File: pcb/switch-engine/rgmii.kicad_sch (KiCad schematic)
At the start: 64 parts, among them J20 0826-1G1T-23-F, Q2 SSM6N58NU, U22 ECS-1612MV-250-CN, U23 KSZ9031RN, U24 ESD224DQAR, U26 ESD224DQAR, U8 XILINX_ULTRASCALEPLUS_B676

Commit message: First iteration of main board PCB schematic is now passing ERC
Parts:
- added C143: 0.47 uF, azonenberg_pcb:EIA_0402_CAP_NOSILK, symbol device:C
- added C144, C145: 0.1 uF, azonenberg_pcb:EIA_0402_CAP_NOSILK, symbol device:C
- added U27: SIT9121AI-2BF-XXS156.250000G, azonenberg_pcb:OSCILLATOR_LVDS_3.2x2.5, symbol osc-azonenberg:OSC_LVDS_NOPAD
- U8: value XILINX_ULTRASCALEPLUS_B676 -> XCKU5P-2FFVB676I
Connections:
- net 3V3: now also C143.1, U27.1 (EN), U27.6 (VDD)
- net GND: now also C143.2, U27.3 (GND)
- net FPGA_CLK_156M25_P: now reaches U8.D19 (IO_L12P_T1U_N10_GC_67)
- net FPGA_CLK_156M25_P: now also C144.2
- net FPGA_CLK_156M25_N: now reaches U8.D20 (IO_L12N_T1U_N11_GC_67)
- net FPGA_CLK_156M25_N: now also C145.2
- new net RC3_N: C145.1, U27.5 (OUT_N)
- new net RC3_P: C144.1, U27.4 (OUT_P)
- no-connect marks 37 -> 35
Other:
- note added: "Clocks"
- note added: "FPGA RGMII"
- note added: "PHY and straps"
- note added: "PHY decoupling"
- note added: "RJ45 and ESD protection"
- note removed: "TODO: add an LVDS oscillator or something for system core clock?"
- company: (none) -> Antikernel Labs
- title: (none) -> LATENTRED Ethernet Switch - Main Board
- moved on the sheet: C111, C112, C113, C114, C115, C116, C117, C118, C119, C120, C121, C122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

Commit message: Added footprints and created initial skeleton of layout
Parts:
- U8: footprint (none) -> azonenberg_pcb:BGA_676_27x27_FULLARRAY_1MM_FFG676
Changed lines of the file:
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@@
 			)
 		)
-		(property "Footprint" ""
+		(property "Footprint" "azonenberg_pcb:BGA_676_27x27_FULLARRAY_1MM_FFG676"
 			(at 392.43 151.13 0)
 			(effects

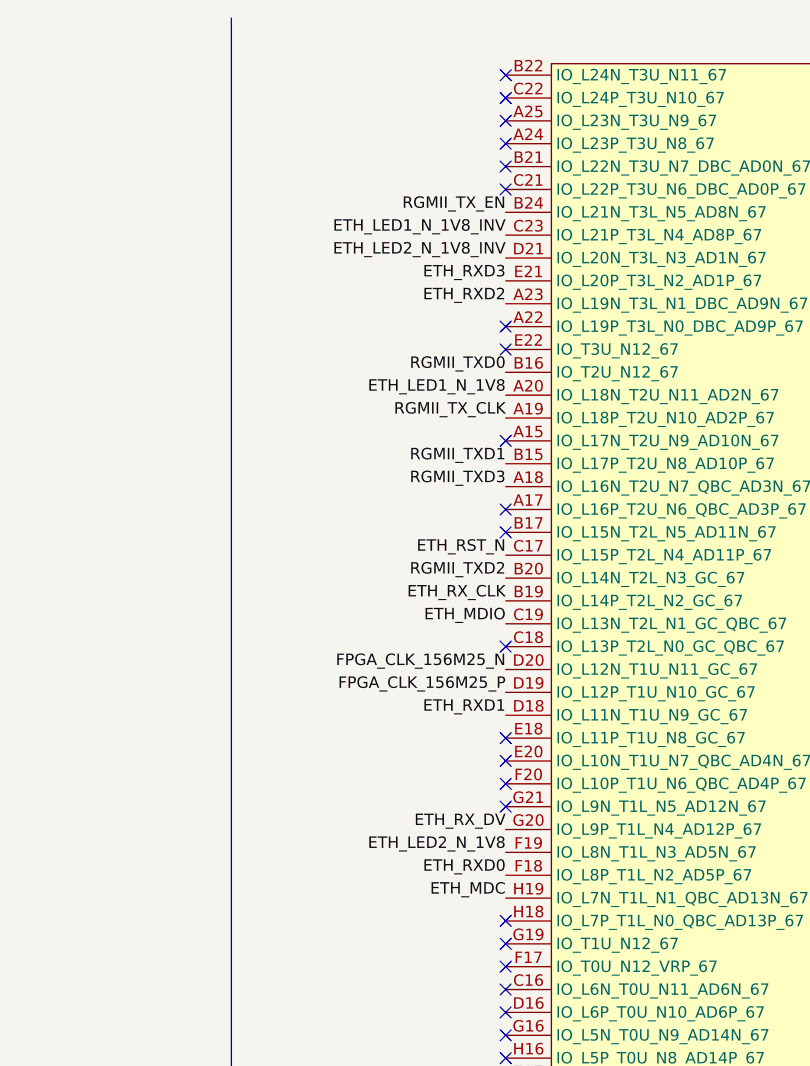
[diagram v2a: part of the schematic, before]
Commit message: Initial routing progress on RGMII and FMC
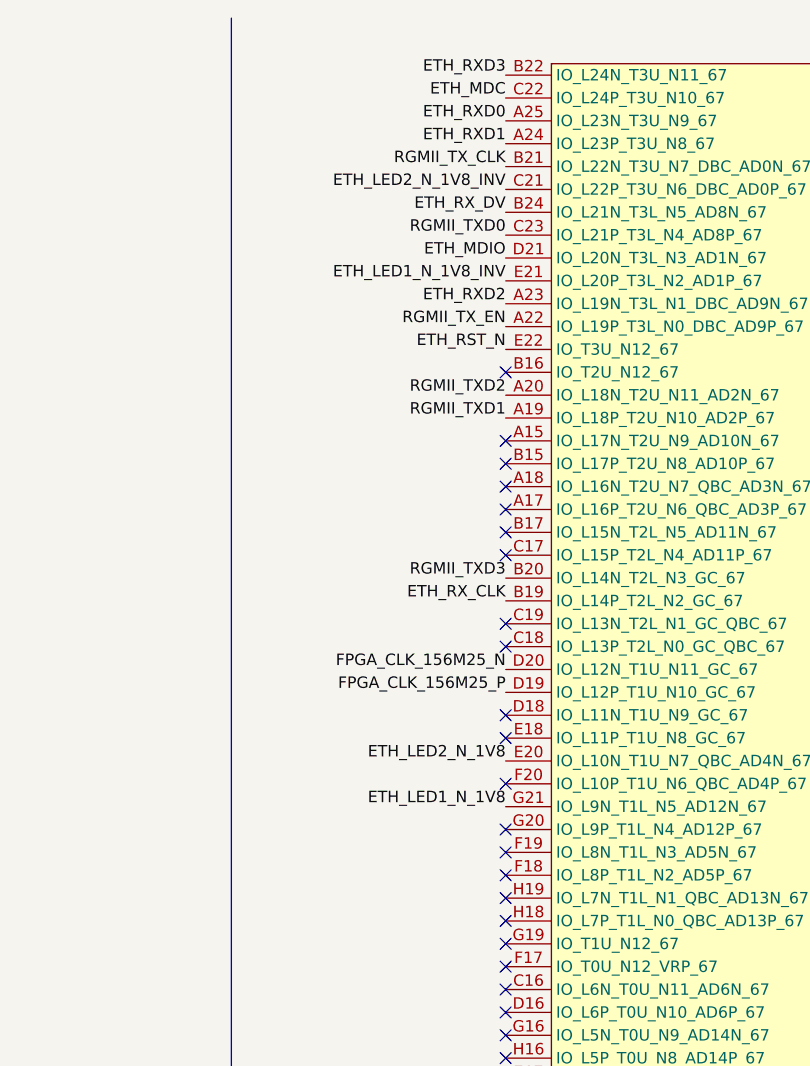
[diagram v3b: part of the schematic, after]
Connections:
- net ETH_LED1_N_1V8: now also U8.G21 (IO_L9N_T1L_N5_AD12N_67); no longer U8.A20 (IO_L18N_T2U_N11_AD2N_67)
- net ETH_LED1_N_1V8_INV: now also U8.E21 (IO_L20P_T3L_N2_AD1P_67); no longer U8.C23 (IO_L21P_T3L_N4_AD8P_67)
- net ETH_LED2_N_1V8: now also U8.E20 (IO_L10N_T1U_N7_QBC_AD4N_67); no longer U8.F19 (IO_L8N_T1L_N3_AD5N_67)
- net ETH_LED2_N_1V8_INV: now also U8.C21 (IO_L22P_T3U_N6_DBC_AD0P_67); no longer U8.D21 (IO_L20N_T3L_N3_AD1N_67)
- net ETH_MDC: now also U8.C22 (IO_L24P_T3U_N10_67); no longer U8.H19 (IO_L7N_T1L_N1_QBC_AD13N_67)
- net ETH_MDIO: now also U8.D21 (IO_L20N_T3L_N3_AD1N_67); no longer U8.C19 (IO_L13N_T2L_N1_GC_QBC_67)
- net ETH_RST_N: now also U8.E22 (IO_T3U_N12_67); no longer U8.C17 (IO_L15P_T2L_N4_AD11P_67)
- net ETH_RXD0: now also U8.A25 (IO_L23N_T3U_N9_67); no longer U8.F18 (IO_L8P_T1L_N2_AD5P_67)
- net ETH_RXD1: now also U8.A24 (IO_L23P_T3U_N8_67); no longer U8.D18 (IO_L11N_T1U_N9_GC_67)
- net ETH_RXD3: now also U8.B22 (IO_L24N_T3U_N11_67); no longer U8.E21 (IO_L20P_T3L_N2_AD1P_67)
- net ETH_RX_DV: now also U8.B24 (IO_L21N_T3L_N5_AD8N_67); no longer U8.G20 (IO_L9P_T1L_N4_AD12P_67)
- net RGMII_TXD0: now also U8.C23 (IO_L21P_T3L_N4_AD8P_67); no longer U8.B16 (IO_T2U_N12_67)
- net RGMII_TXD1: now also U8.A19 (IO_L18P_T2U_N10_AD2P_67); no longer U8.B15 (IO_L17P_T2U_N8_AD10P_67)
- net RGMII_TXD2: now also U8.A20 (IO_L18N_T2U_N11_AD2N_67); no longer U8.B20 (IO_L14N_T2L_N3_GC_67)
- net RGMII_TXD3: now also U8.B20 (IO_L14N_T2L_N3_GC_67); no longer U8.A18 (IO_L16N_T2U_N7_QBC_AD3N_67)
- net RGMII_TX_CLK: now also U8.B21 (IO_L22N_T3U_N7_DBC_AD0N_67); no longer U8.A19 (IO_L18P_T2U_N10_AD2P_67)
- net RGMII_TX_EN: now also U8.A22 (IO_L19P_T3L_N0_DBC_AD9P_67); no longer U8.B24 (IO_L21N_T3L_N5_AD8N_67)
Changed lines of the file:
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@@
 	(title_block
 		(title "LATENTRED Ethernet Switch - Main Board")
-		(date "2025-06-02")
+		(date "2025-06-04")
 		(rev "0.1")
 		(company "Antikernel Labs")
@@
 	)
 	(no_connect
-		(at 323.85 19.05)
+		(at 323.85 102.87)
 	)
 	(no_connect
@@
 	)
 	(no_connect
+		(at 323.85 118.11)
+	)
+	(no_connect
+		(at 323.85 64.77)
+	)
+	(no_connect
+		(at 323.85 59.69)
+	)
+	(no_connect
+		(at 323.85 120.65)
+	)
+	(no_connect
+		(at 323.85 92.71)
+	)
+	(no_connect
+		(at 323.85 148.59)
+	)
+	(no_connect
+		(at 323.85 130.81)
+	)
+	(no_connect
+		(at 323.85 105.41)
+	)
+	(no_connect
+		(at 323.85 69.85)
+	)
+	(no_connect
+		(at 323.85 90.17)
+	)
+	(no_connect
 		(at 323.85 97.79)
 	)
 	(no_connect
-		(at 323.85 100.33)
-	)
-	(no_connect
-		(at 323.85 118.11)
-	)
-	(no_connect
-		(at 323.85 26.67)
-	)
-	(no_connect
-		(at 323.85 59.69)
-	)
-	(no_connect
-		(at 323.85 120.65)
-	)
-	(no_connect
-		(at 323.85 92.71)
-	)
-	(no_connect
-		(at 323.85 148.59)
-	)
-	(no_connect
-		(at 323.85 130.81)
-	)
-	(no_connect
-		(at 323.85 69.85)
-	)
-	(no_connect
-		(at 323.85 95.25)
-	)
-	(no_connect
 		(at 323.85 115.57)
 	)
@@
 	)
 	(no_connect
-		(at 323.85 49.53)
-	)
-	(no_connect
 		(at 323.85 146.05)
 	)
@@
 	)
 	(no_connect
-		(at 323.85 24.13)
-	)
-	(no_connect
-		(at 323.85 46.99)
-	)
-	(no_connect
 		(at 323.85 151.13)
 	)
@@
 	)
 	(no_connect
-		(at 323.85 31.75)
-	)
-	(no_connect
-		(at 323.85 29.21)
-	)
-	(no_connect
 		(at 323.85 140.97)
 	)
@@
 	)
 	(no_connect
+		(at 323.85 80.01)
+	)
+	(no_connect
+		(at 323.85 110.49)
+	)
+	(no_connect
+		(at 323.85 62.23)
+	)
+	(no_connect
+		(at 323.85 107.95)
+	)
+	(no_connect
 		(at 323.85 113.03)
 	)
 	(no_connect
-		(at 323.85 21.59)
+		(at 323.85 72.39)
+	)
+	(no_connect
+		(at 323.85 52.07)
 	)
 	(wire
@@
 	)
 	(label "ETH_RST_N"
-		(at 323.85 72.39 180)
+		(at 323.85 49.53 180)
 		(fields_autoplaced yes)
 		(effects
@@
 	)
 	(label "RGMII_TXD0"
-		(at 323.85 52.07 180)
+		(at 323.85 36.83 180)
 		(fields_autoplaced yes)
 		(effects
@@
 	)
 	(label "ETH_LED2_N_1V8"
-		(at 323.85 105.41 180)
+		(at 323.85 95.25 180)
 		(fields_autoplaced yes)
 		(effects
@@
 	)
 	(label "ETH_RXD0"
-		(at 323.85 107.95 180)
+		(at 323.85 24.13 180)
 		(fields_autoplaced yes)
 		(effects
@@
 	)
 	(label "RGMII_TXD2"
-		(at 323.85 74.93 180)
+		(at 323.85 54.61 180)
 		(fields_autoplaced yes)
 		(effects
@@
 	)
 	(label "ETH_RX_DV"
-		(at 323.85 102.87 180)
+		(at 323.85 34.29 180)
 		(fields_autoplaced yes)
 		(effects
@@
 	)
 	(label "RGMII_TX_EN"
-		(at 323.85 34.29 180)
+		(at 323.85 46.99 180)
 		(fields_autoplaced yes)
 		(effects
@@
 	)
 	(label "ETH_MDC"
-		(at 323.85 110.49 180)
+		(at 323.85 21.59 180)
 		(fields_autoplaced yes)
 		(effects
@@
 	)
 	(label "ETH_RXD1"
-		(at 323.85 90.17 180)
+		(at 323.85 26.67 180)
 		(fields_autoplaced yes)
 		(effects
@@
 	)
 	(label "RGMII_TX_CLK"
-		(at 323.85 57.15 180)
+		(at 323.85 29.21 180)
 		(fields_autoplaced yes)
 		(effects
@@
 	)
 	(label "RGMII_TXD1"
-		(at 323.85 62.23 180)
+		(at 323.85 57.15 180)
 		(fields_autoplaced yes)
 		(effects
@@
 	)
 	(label "ETH_RXD3"
-		(at 323.85 41.91 180)
+		(at 323.85 19.05 180)
 		(fields_autoplaced yes)
 		(effects
@@
 	)
 	(label "ETH_LED1_N_1V8"
-		(at 323.85 54.61 180)
+		(at 323.85 100.33 180)
 		(fields_autoplaced yes)
 		(effects
@@
 	)
 	(label "ETH_LED2_N_1V8_INV"
+		(at 323.85 31.75 180)
+		(fields_autoplaced yes)
+		(effects
+			(font
+				(size 1.27 1.27)
+			)
+			(justify right bottom)
+		)
+	)
+	(label "ETH_MDIO"
 		(at 323.85 39.37 180)
-		(fields_autoplaced yes)
-		(effects
-			(font
-				(size 1.27 1.27)
-			)
-			(justify right bottom)
-		)
-	)
-	(label "ETH_MDIO"
-		(at 323.85 80.01 180)
 		(fields_autoplaced yes)
 		(effects
@@
 	)
 	(label "RGMII_TXD3"
-		(at 323.85 64.77 180)
+		(at 323.85 74.93 180)
 		(fields_autoplaced yes)
 		(effects
@@
 	)
 	(label "ETH_LED1_N_1V8_INV"
-		(at 323.85 36.83 180)
-		(fields_autoplaced yes)
-		(effects
+		(at 323.85 41.91 180)
+		(fields_autoplaced yes)
+		(effects

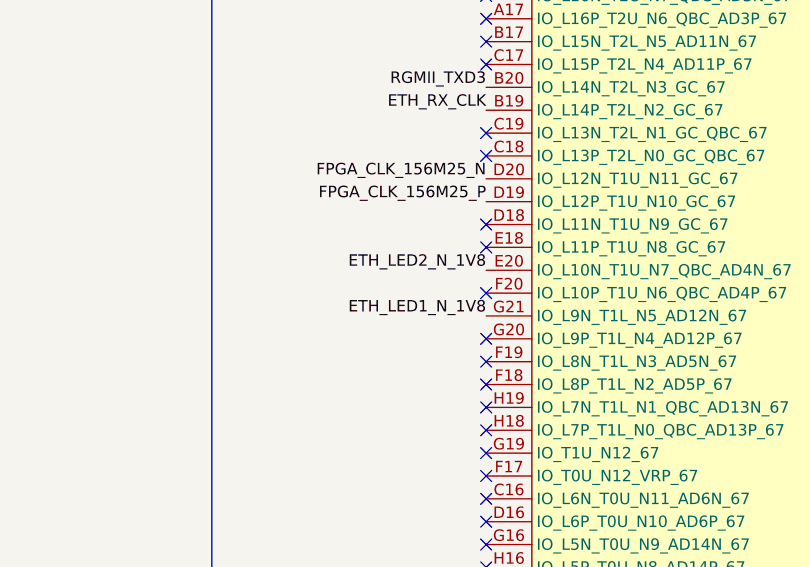
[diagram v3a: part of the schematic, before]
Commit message: Continued layout of MCU area, added cutout for fan
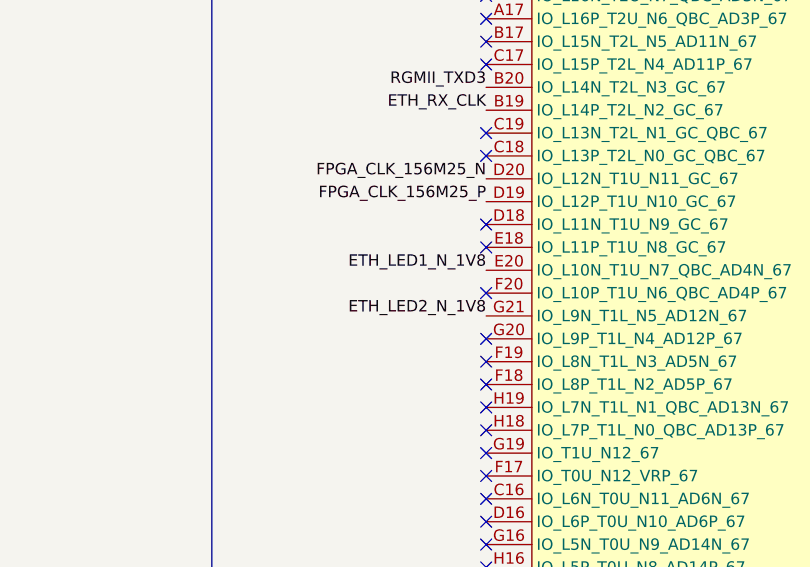
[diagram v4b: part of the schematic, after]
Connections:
- net ETH_LED1_N_1V8: now also U8.E20 (IO_L10N_T1U_N7_QBC_AD4N_67); no longer U8.G21 (IO_L9N_T1L_N5_AD12N_67)
- net ETH_LED2_N_1V8: now also U8.G21 (IO_L9N_T1L_N5_AD12N_67); no longer U8.E20 (IO_L10N_T1U_N7_QBC_AD4N_67)
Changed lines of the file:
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@@
 	(title_block
 		(title "LATENTRED Ethernet Switch - Main Board")
-		(date "2025-06-04")
+		(date "2025-06-06")
 		(rev "0.1")
 		(company "Antikernel Labs")
@@
 	)
 	(label "ETH_LED2_N_1V8"
-		(at 323.85 95.25 180)
+		(at 323.85 100.33 180)
 		(fields_autoplaced yes)
 		(effects
@@
 	)
 	(label "ETH_LED1_N_1V8"
-		(at 323.85 100.33 180)
-		(fields_autoplaced yes)
-		(effects
+		(at 323.85 95.25 180)
+		(fields_autoplaced yes)
+		(effects

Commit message: Lots of routing cleanup around MCU
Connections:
- net ETH_LED1_N_1V8_INV: now also U8.C21 (IO_L22P_T3U_N6_DBC_AD0P_67); no longer U8.E21 (IO_L20P_T3L_N2_AD1P_67)
- net ETH_LED2_N_1V8: now also U8.E21 (IO_L20P_T3L_N2_AD1P_67); no longer U8.G21 (IO_L9N_T1L_N5_AD12N_67)
- net ETH_LED2_N_1V8_INV: now also U8.C23 (IO_L21P_T3L_N4_AD8P_67); no longer U8.C21 (IO_L22P_T3U_N6_DBC_AD0P_67)
- net RGMII_TXD0: now also U8.G21 (IO_L9N_T1L_N5_AD12N_67); no longer U8.C23 (IO_L21P_T3L_N4_AD8P_67)
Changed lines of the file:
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@@
 	)
 	(label "RGMII_TXD0"
-		(at 323.85 36.83 180)
+		(at 323.85 100.33 180)
 		(fields_autoplaced yes)
 		(effects
@@
 	)
 	(label "ETH_LED2_N_1V8"
-		(at 323.85 100.33 180)
+		(at 323.85 41.91 180)
 		(fields_autoplaced yes)
 		(effects
@@
 	)
 	(label "ETH_LED2_N_1V8_INV"
-		(at 323.85 31.75 180)
+		(at 323.85 36.83 180)
 		(fields_autoplaced yes)
 		(effects
@@
 	)
 	(label "ETH_LED1_N_1V8_INV"
-		(at 323.85 41.91 180)
-		(fields_autoplaced yes)
-		(effects
+		(at 323.85 31.75 180)
+		(fields_autoplaced yes)
+		(effects
